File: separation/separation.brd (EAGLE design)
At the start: 9 parts, among them IC1 L7805ACV

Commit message: create dimension
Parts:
- moved JP1 0.76 mm to (127.1, 54.9)
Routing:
- net VBAT: track 38.8 -> 38.0 mm
- net SERVO: track 23.8 -> 23.0 mm
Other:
- board outline added: 71.1 x 26.7 mm
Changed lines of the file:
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@@
 <wire x1="98.298" y1="75.311" x2="98.298" y2="54.991" width="0.254" layer="21"/>
 <wire x1="98.298" y1="54.991" x2="100.838" y2="52.451" width="0.254" layer="21" curve="90"/>
+<wire x1="78.74" y1="78.74" x2="149.86" y2="78.74" width="0.508" layer="20"/>
+<wire x1="149.86" y1="78.74" x2="149.86" y2="52.07" width="0.508" layer="20"/>
+<wire x1="149.86" y1="52.07" x2="78.74" y2="52.07" width="0.508" layer="20"/>
+<wire x1="78.74" y1="52.07" x2="78.74" y2="78.74" width="0.508" layer="20"/>
 </plain>
 <attributes>
@@
 <attribute name="VALUE" x="143.51" y="59.69" size="1.27" layer="27" align="center"/>
 </element>
-<element name="JP1" library="pinhead" library_urn="urn:adsk.eagle:library:325" package="1X03" package3d_urn="urn:adsk.eagle:package:22458/2" value="" x="127.127" y="54.102" smashed="yes">
-<attribute name="NAME" x="123.2408" y="55.9308" size="1.27" layer="25" ratio="10"/>
-<attribute name="POPULARITY" value="92" x="127.127" y="54.102" size="1.778" layer="27" font="vector" ratio="15" display="off"/>
-<attribute name="VALUE" x="123.317" y="50.927" size="1.27" layer="27"/>
+<element name="JP1" library="pinhead" library_urn="urn:adsk.eagle:library:325" package="1X03" package3d_urn="urn:adsk.eagle:package:22458/2" value="" x="127.127" y="54.864" smashed="yes">
+<attribute name="NAME" x="123.2408" y="56.6928" size="1.27" layer="25" ratio="10"/>
+<attribute name="POPULARITY" value="92" x="127.127" y="54.864" size="1.778" layer="27" font="vector" ratio="15" display="off"/>
+<attribute name="VALUE" x="123.317" y="51.689" size="1.27" layer="27"/>
 </element>
 <element name="PAD1" library="wirepad" library_urn="urn:adsk.eagle:library:412" package="3,17/1,1" package3d_urn="urn:adsk.eagle:package:30832/1" value="WIREPAD3,17/1,1" x="146.05" y="68.58" smashed="yes">
@@
 <wire x1="147.51" y1="59.69" x2="134.62" y2="72.5805" width="0" layer="19" extent="1-1"/>
 <wire x1="140.97" y1="72.4" x2="134.62" y2="72.5805" width="0" layer="19" extent="1-1"/>
-<wire x1="127.127" y1="54.102" x2="140.97" y2="72.4" width="0" layer="19" extent="1-1"/>
-<wire x1="146.05" y1="74.93" x2="127.127" y2="54.102" width="0" layer="19" extent="1-1"/>
+<wire x1="127.127" y1="54.864" x2="140.97" y2="72.4" width="0" layer="19" extent="1-1"/>
+<wire x1="146.05" y1="74.93" x2="127.127" y2="54.864" width="0" layer="19" extent="1-1"/>
 </signal>
 <signal name="A1">
@@
 <contactref element="JP1" pad="3"/>
 <wire x1="119.5705" y1="69.85" x2="119.38" y2="70.0405" width="0.508" layer="1"/>
-<wire x1="129.667" y1="54.102" x2="129.54" y2="54.229" width="0.508" layer="1"/>
-<wire x1="129.54" y1="54.229" x2="129.54" y2="55.88" width="0.508" layer="1"/>
+<wire x1="129.667" y1="54.864" x2="129.54" y2="54.991" width="0.508" layer="1"/>
+<wire x1="129.54" y1="54.991" x2="129.54" y2="55.88" width="0.508" layer="1"/>
 <wire x1="129.54" y1="55.88" x2="128.27" y2="57.15" width="0.508" layer="1"/>
 <wire x1="128.27" y1="57.15" x2="124.46" y2="57.15" width="0.508" layer="1"/>
@@
 <wire x1="146.05" y1="68.58" x2="142.24" y2="68.58" width="1.27" layer="1"/>
 <wire x1="142.24" y1="68.58" x2="140.97" y2="69.85" width="1.27" layer="1"/>
-<wire x1="124.587" y1="54.102" x2="124.46" y2="54.229" width="1.27" layer="16"/>
-<wire x1="124.46" y1="54.229" x2="124.46" y2="55.88" width="1.27" layer="16"/>
+<wire x1="124.587" y1="54.864" x2="124.46" y2="54.991" width="1.27" layer="16"/>
+<wire x1="124.46" y1="54.991" x2="124.46" y2="55.88" width="1.27" layer="16"/>
 <wire x1="124.46" y1="55.88" x2="125.73" y2="57.15" width="1.27" layer="16"/>
 <wire x1="125.73" y1="57.15" x2="142.24" y2="57.15" width="1.27" layer="16"/>

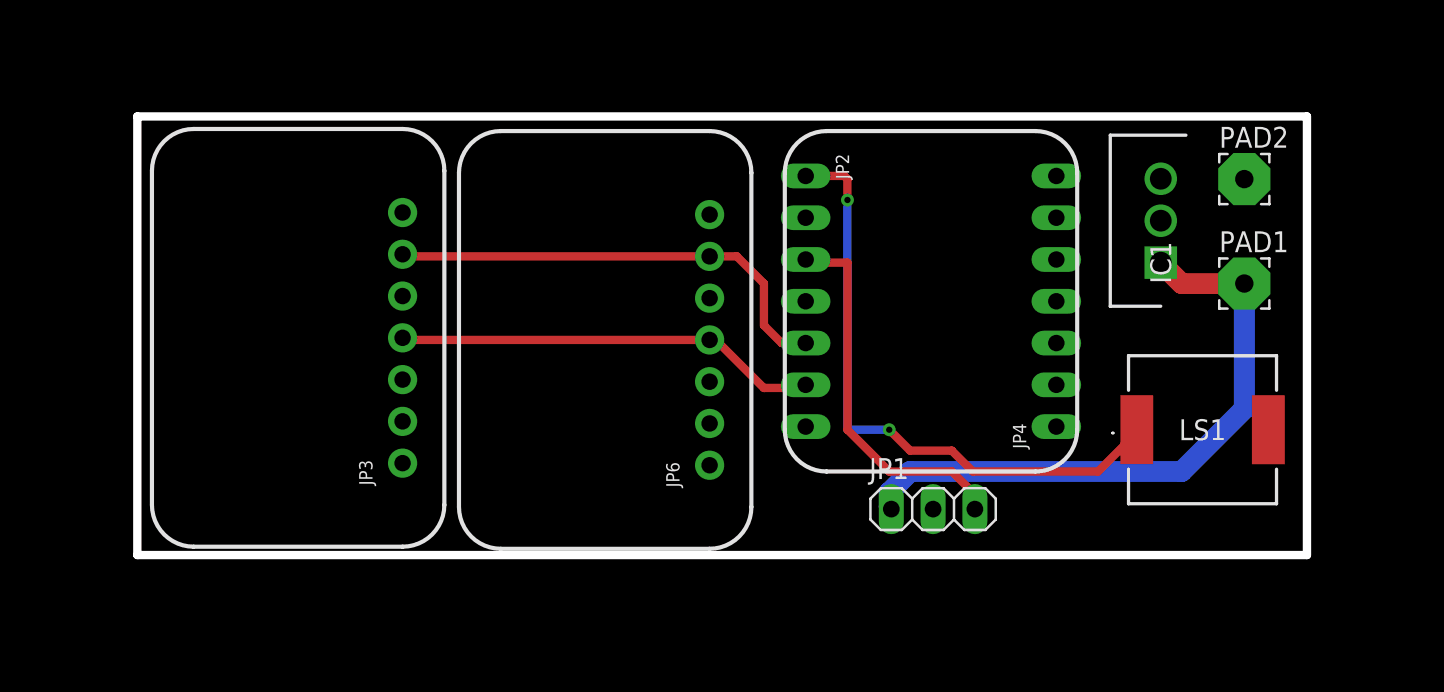
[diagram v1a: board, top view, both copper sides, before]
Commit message: create gnd plane on top layer
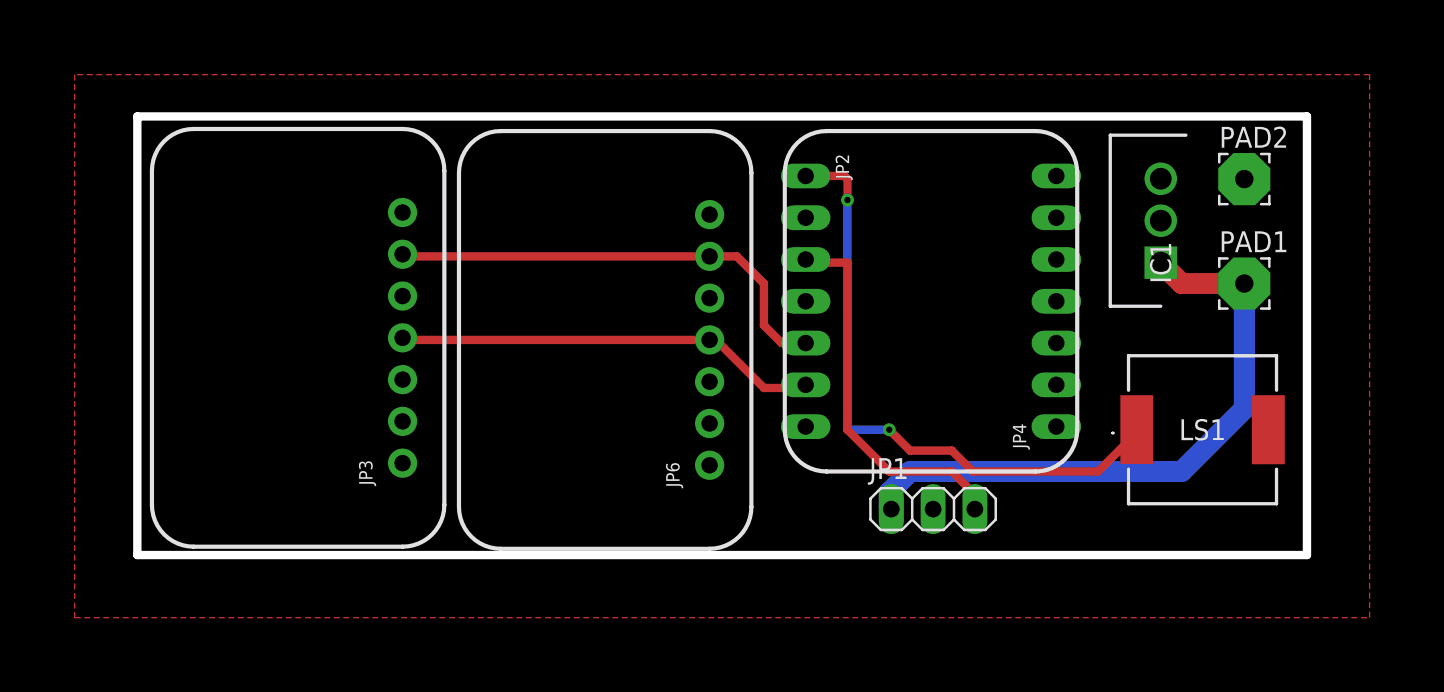
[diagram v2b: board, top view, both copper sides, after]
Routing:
- added copper zone on layer 1, net GND
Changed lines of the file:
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@@
 <contactref element="JP1" pad="2"/>
 <contactref element="PAD2" pad="1"/>
+<polygon width="0.508" layer="1" isolate="0.3048">
+<vertex x="74.93" y="81.28"/>
+<vertex x="74.93" y="48.26"/>
+<vertex x="153.67" y="48.26"/>
+<vertex x="153.67" y="81.28"/>
+</polygon>
+<wire x1="140.97" y1="72.4" x2="146.05" y2="74.93" width="0" layer="19" extent="1-1"/>
+<wire x1="134.62" y1="72.5805" x2="140.97" y2="72.4" width="0" layer="19" extent="1-1"/>
+<wire x1="147.51" y1="59.69" x2="140.97" y2="72.4" width="0" layer="19" extent="1-1"/>
+<wire x1="127.127" y1="54.864" x2="134.62" y2="72.5805" width="0" layer="19" extent="1-1"/>
+<wire x1="113.538" y1="62.611" x2="127.127" y2="54.864" width="0" layer="19" extent="1-1"/>
 <wire x1="94.869" y1="62.738" x2="113.538" y2="62.611" width="0" layer="19" extent="1-1"/>
-<wire x1="134.62" y1="72.5805" x2="94.869" y2="62.738" width="0" layer="19" extent="1-1"/>
-<wire x1="147.51" y1="59.69" x2="134.62" y2="72.5805" width="0" layer="19" extent="1-1"/>
-<wire x1="140.97" y1="72.4" x2="134.62" y2="72.5805" width="0" layer="19" extent="1-1"/>
-<wire x1="127.127" y1="54.864" x2="140.97" y2="72.4" width="0" layer="19" extent="1-1"/>
-<wire x1="146.05" y1="74.93" x2="127.127" y2="54.864" width="0" layer="19" extent="1-1"/>
 </signal>
 <signal name="A1">

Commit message: create vcc plane on bottom layer
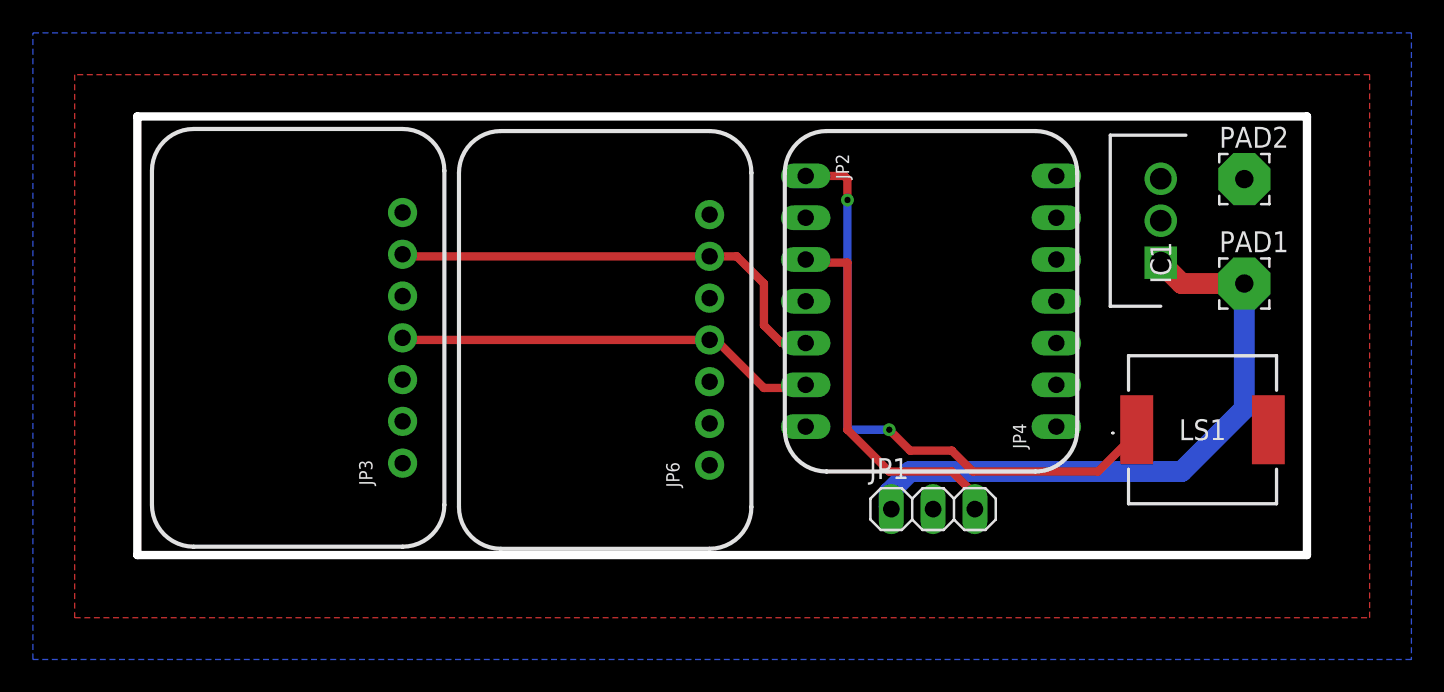
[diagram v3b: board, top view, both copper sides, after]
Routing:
- added copper zone on layer 16, net VCC
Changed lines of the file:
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@@
 <contactref element="JP6" pad="1"/>
 <contactref element="IC1" pad="3"/>
+<polygon width="0.508" layer="16" isolate="0.3048">
+<vertex x="72.39" y="83.82"/>
+<vertex x="156.21" y="83.82"/>
+<vertex x="156.21" y="45.72"/>
+<vertex x="72.39" y="45.72"/>
+</polygon>
+<wire x1="134.62" y1="75.1205" x2="140.97" y2="74.95" width="0" layer="19" extent="1-1"/>
+<wire x1="113.538" y1="57.531" x2="134.62" y2="75.1205" width="0" layer="19" extent="1-1"/>
 <wire x1="94.869" y1="57.658" x2="113.538" y2="57.531" width="0" layer="19" extent="1-1"/>
-<wire x1="134.62" y1="75.1205" x2="94.869" y2="57.658" width="0" layer="19" extent="1-1"/>
-<wire x1="140.97" y1="74.95" x2="94.869" y2="57.658" width="0" layer="19" extent="1-1"/>
 </signal>
 <signal name="PB22/I6/SERCOM5.1">
